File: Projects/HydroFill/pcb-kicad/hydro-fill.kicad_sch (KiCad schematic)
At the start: 27 parts, among them J1 12V 5A, J2 Solenoid output, J3 Pressure transmitter, J4 Temperature, J5 Display TFT 1.77'', J6 Status LEDs, J7 Manual Start Btn, Q1 S8050, Q2 S8050, Q3 IRFZ44N, Q4 S8050

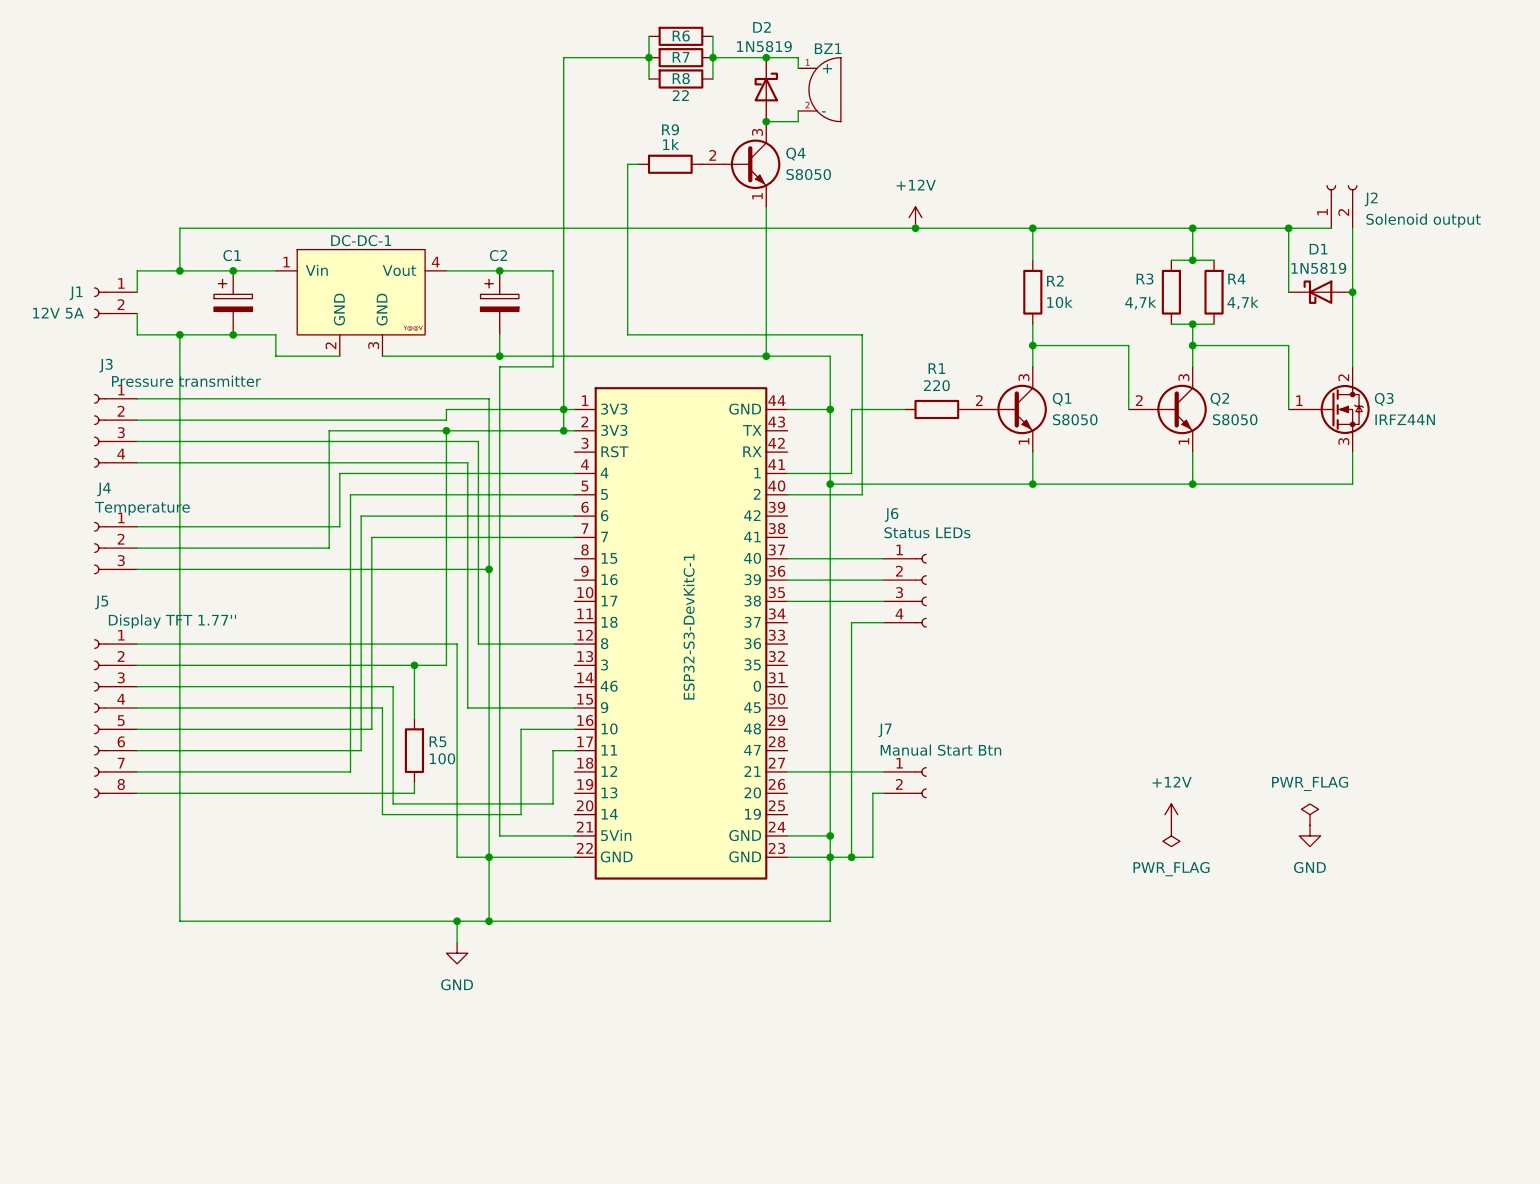
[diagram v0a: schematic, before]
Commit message: [HydroFiller][PCB] Add `ESP Power Of When USB connected` connector
- Remove 1000mF capacitor
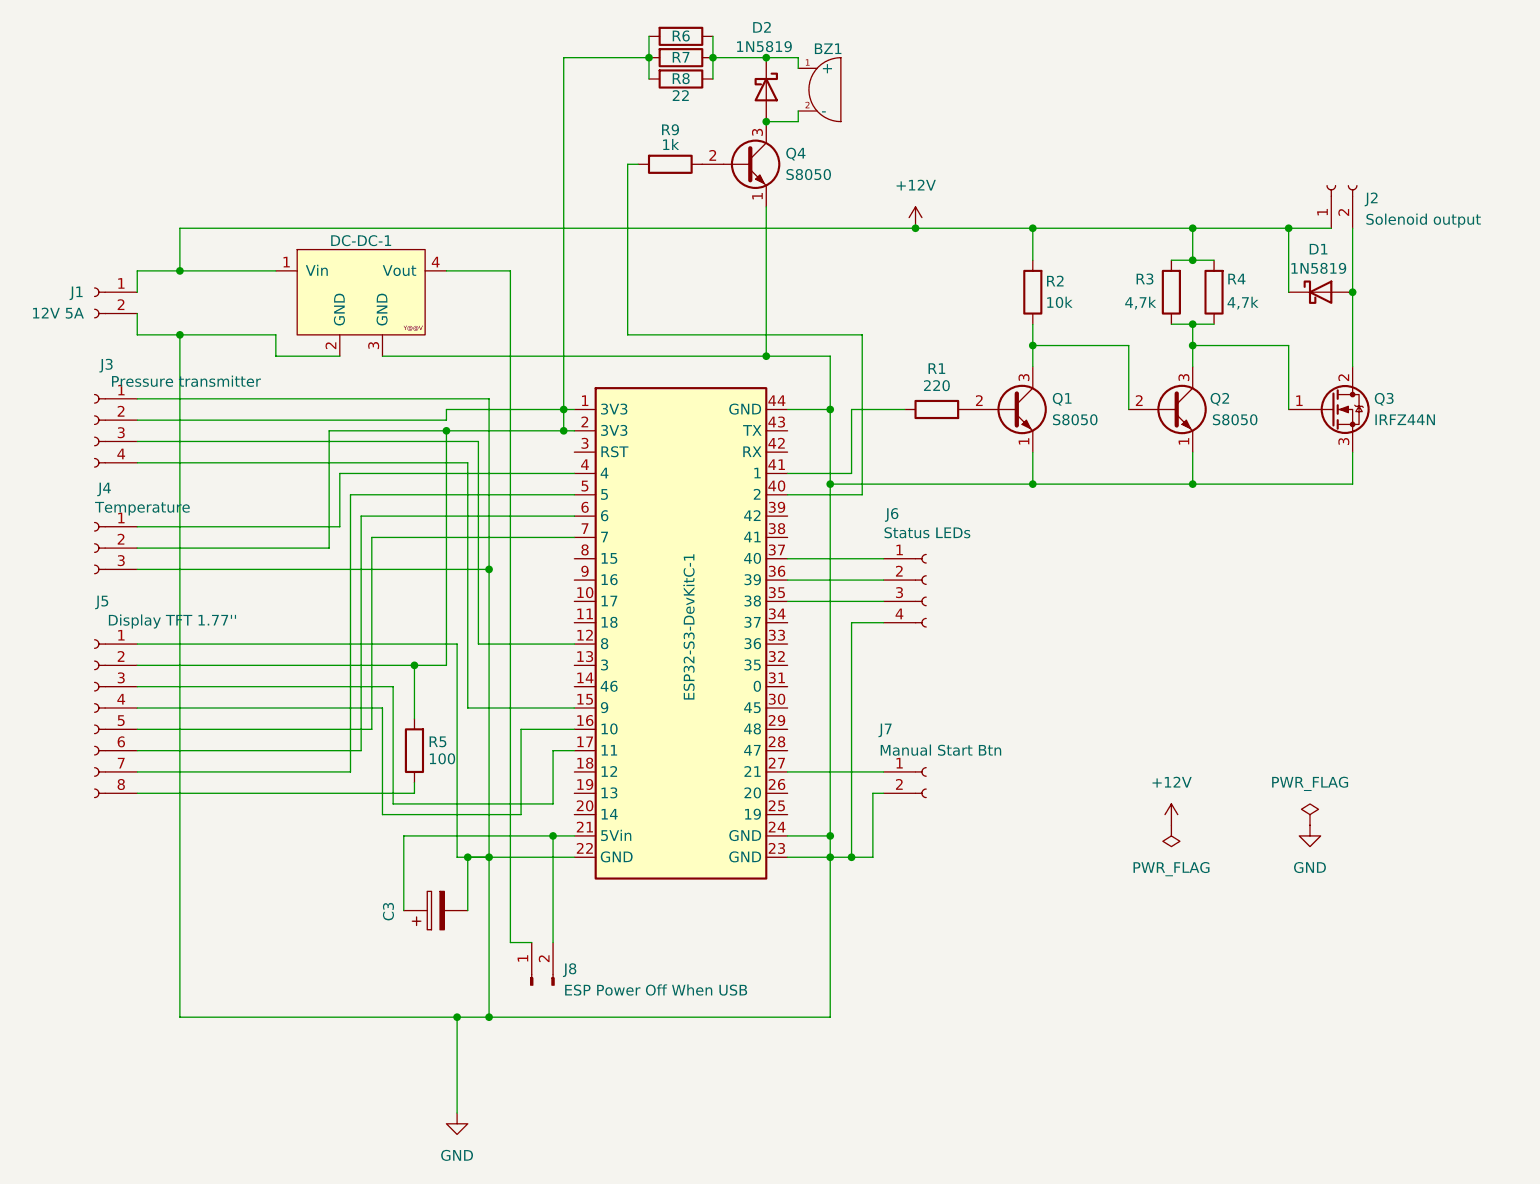
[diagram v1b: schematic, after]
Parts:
- removed C1: 1000uF 25V, Capacitor_THT:CP_Radial_D10.0mm_P5.00mm, symbol Device:C_Polarized
- removed C2: 470uF 16V, Capacitor_THT:CP_Radial_D8.0mm_P3.50mm, symbol Device:C_Polarized
- added C3: 470uF 16V, Capacitor_THT:CP_Radial_D8.0mm_P3.50mm, symbol Device:C_Polarized
- added J8: ESP Power Off When USB, symbol Connector:Conn_01x02_Pin
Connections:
- net GND: now also C3.2
- net at DC-DC-1.4 (Vout): now also J8.1 (Pin_1); no longer ESP32-S3-DevKitC-1.21 (5Vin)
- new net: C3.1, ESP32-S3-DevKitC-1.21 (5Vin), J8.2 (Pin_2)

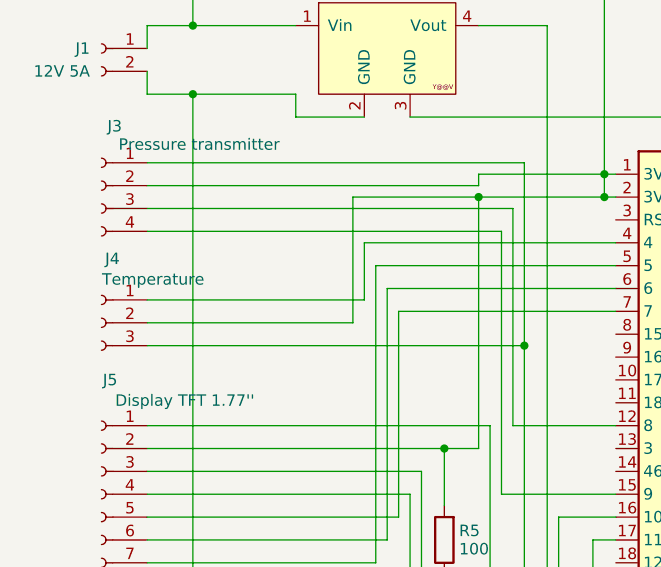
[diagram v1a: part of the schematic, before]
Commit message: [HydroFiller][PCB] Add resistor 4.7kOm to out of temperature sensor
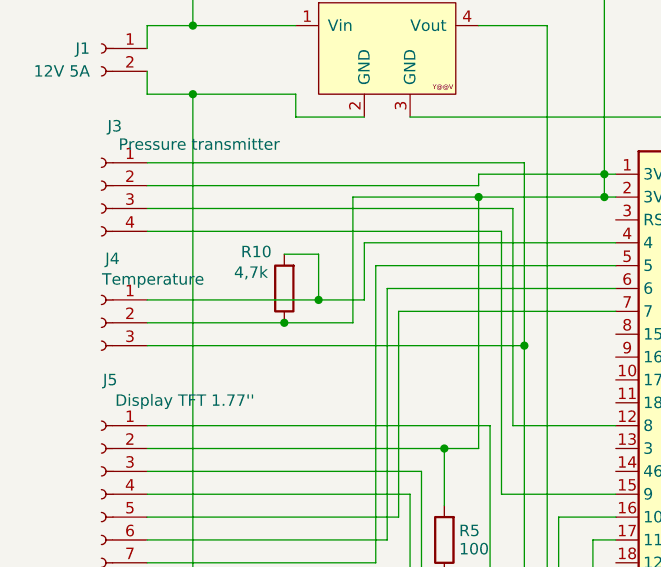
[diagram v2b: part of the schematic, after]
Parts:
- added R10: 4,7k, Resistor_THT:R_Axial_DIN0204_L3.6mm_D1.6mm_P7.62mm_Horizontal, symbol Device:R
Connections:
- net at ESP32-S3-DevKitC-1.1 (3V3), ESP32-S3-DevKitC-1.2 (3V3), J3.2 (Pin_2)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: now also R10.1
- net at ESP32-S3-DevKitC-1.4, J4.1 (Pin_1): now also R10.2
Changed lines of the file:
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@@
 	)
 	(junction
+		(at 85.09 87.63)
+		(diameter 0)
+		(color 0 0 0 0)
+	)
+	(junction
 		(at 130.81 29.21)
 		(diameter 0)
@@
 		(color 0 0 0 0)
 	)
+	(junction
+		(at 88.9 85.09)
+		(diameter 0)
+		(color 0 0 0 0)
+	)
 	(wire
 		(pts
@@
 	(wire
 		(pts
-			(xy 69.85 85.09) (xy 93.98 85.09)
+			(xy 69.85 85.09) (xy 88.9 85.09)
 		)
 		(stroke
@@
 	(wire
 		(pts
+			(xy 88.9 80.01) (xy 88.9 85.09)
+		)
+		(stroke
+			(width 0)
+			(type default)
+		)
+	)
+	(wire
+		(pts
 			(xy 69.85 109.22) (xy 97.79 109.22)
 		)
@@
 	(wire
 		(pts
-			(xy 69.85 87.63) (xy 92.71 87.63)
+			(xy 69.85 87.63) (xy 85.09 87.63)
 		)
 		(stroke
@@
 	(wire
 		(pts
+			(xy 85.09 87.63) (xy 92.71 87.63)
+		)
+		(stroke
+			(width 0)
+			(type default)
+		)
+	)
+	(wire
+		(pts
 			(xy 109.22 106.68) (xy 121.92 106.68)
 		)
@@
 	(wire
 		(pts
+			(xy 85.09 80.01) (xy 88.9 80.01)
+		)
+		(stroke
+			(width 0)
+			(type default)
+		)
+	)
+	(wire
+		(pts
 			(xy 69.85 72.39) (xy 106.68 72.39)
 		)
@@
 	(wire
 		(pts
+			(xy 88.9 85.09) (xy 93.98 85.09)
+		)
+		(stroke
+			(width 0)
+			(type default)
+		)
+	)
+	(wire
+		(pts
 			(xy 154.94 124.46) (xy 152.4 124.46)
 		)
@@
 					(unit 1)
 				)
+			)
+		)
+	)
+	(symbol
+		(lib_id "Device:R")
+		(at 85.09 83.82 180)
+		(unit 1)
+		(exclude_from_sim no)
+		(in_bom yes)
+		(on_board yes)
+		(dnp no)
+		(property "Reference" "R10"
+			(at 80.264 79.756 0)
+			(effects
+				(font
+					(size 1.27 1.27)
+				)
+				(justify right)
+			)
+		)
+		(property "Value" "4,7k"
+			(at 79.502 82.042 0)
+			(effects
+				(font
+					(size 1.27 1.27)
+				)
+				(justify right)
+			)
+		)
+		(property "Footprint" "Resistor_THT:R_Axial_DIN0204_L3.6mm_D1.6mm_P7.62mm_Horizontal"
+			(at 86.868 83.82 90)
+			(effects
+				(font
+					(size 1.27 1.27)
+				)
+				(hide yes)
+			)
+		)
+		(property "Datasheet" "~"
+			(at 85.09 83.82 0)
+			(effects
+				(font
+					(size 1.27 1.27)
+				)
+				(hide yes)
+			)
+		)
+		(property "Description" "Resistor"
+			(at 85.09 83.82 0)
+			(effects
+				(font
+					(size 1.27 1.27)
+				)
+				(hide yes)
+			)
+		)
+		(pin "2"
+		)
+		(pin "1"
+		)
+		(instances
+			(project "hydro-fill"
+				(path "/d3141547-f75e-4d8b-a0b1-7433a6d75615"
+					(reference "R10")
+					(unit 1)
+				)
